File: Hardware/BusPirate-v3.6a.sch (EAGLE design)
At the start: 45 parts, among them J1 USB-MINIB-5PIN, U1 MIC5205 3V3, U2 MIC5205 3V3, U3 PIC24FJ64GA002, U4 MIC5205 5V0, U5 FT232RL-BASICSSOP, U6 4066

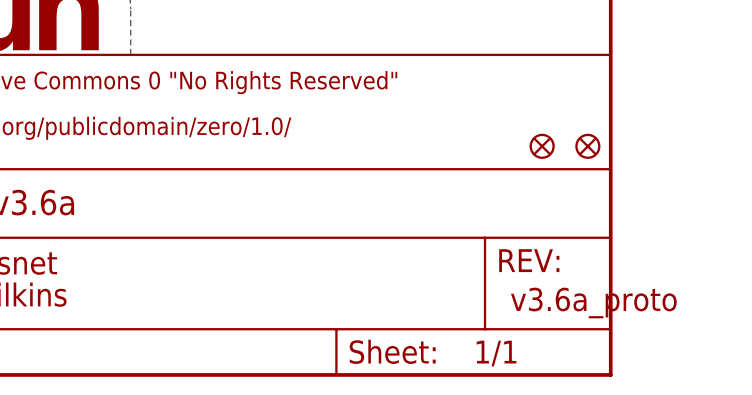
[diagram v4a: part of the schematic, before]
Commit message: Imported DP PCB part, and changed DRC to allow mask to cover large vias.
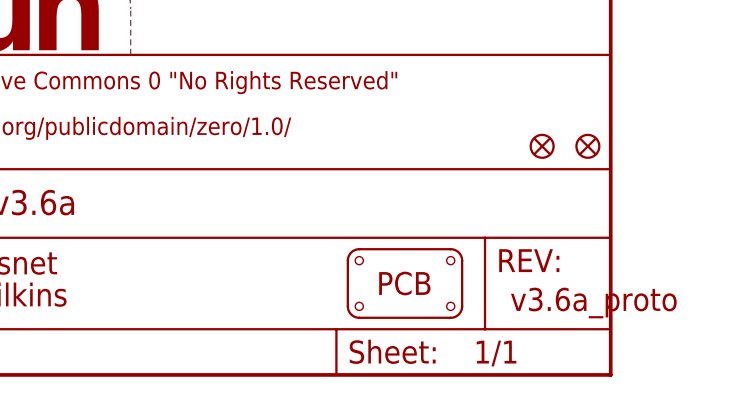
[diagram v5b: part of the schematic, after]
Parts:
- added PCB1: PCB_DP_RECTANGLE-37X60, SparkFun-Boards:PCB_DP_RECTANGLE-37X60
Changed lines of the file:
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@@
 <layer number="113" name="IDFDebug" color="4" fill="1" visible="yes" active="yes"/>
 <layer number="114" name="Badge_Outline" color="11" fill="1" visible="no" active="no"/>
+<layer number="115" name="ReferenceISLANDS" color="7" fill="1" visible="yes" active="yes"/>
 <layer number="116" name="Patch_BOT" color="9" fill="4" visible="yes" active="yes"/>
 <layer number="118" name="Rect_Pads" color="7" fill="1" visible="yes" active="yes"/>
@@
 <part name="C4" library="SparkFun-Capacitors" deviceset="10UF10V10%(0805)" device="" value="10uF"/>
 <part name="GND19" library="SparkFun-Aesthetics" deviceset="GND" device=""/>
+<part name="PCB1" library="SparkFun-Boards" deviceset="PCB_DP_RECTANGLE" device="-37X60"/>
 </parts>
 <sheets>
@@
 <instance part="C4" gate="G$1" x="30.48" y="114.3"/>
 <instance part="GND19" gate="1" x="109.22" y="15.24" rot="MR0"/>
+<instance part="PCB1" gate="G$1" x="226.06" y="10.16"/>
 </instances>
 <busses>

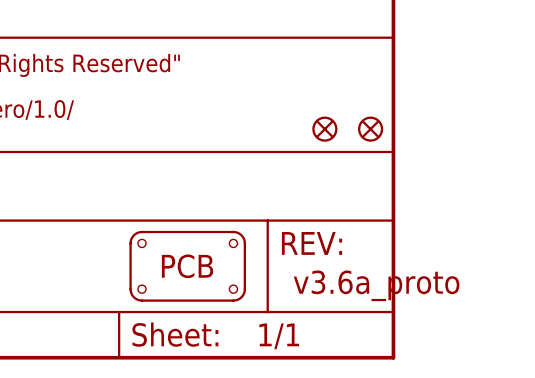
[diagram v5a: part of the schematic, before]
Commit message: Changed one PROD_ID and version number
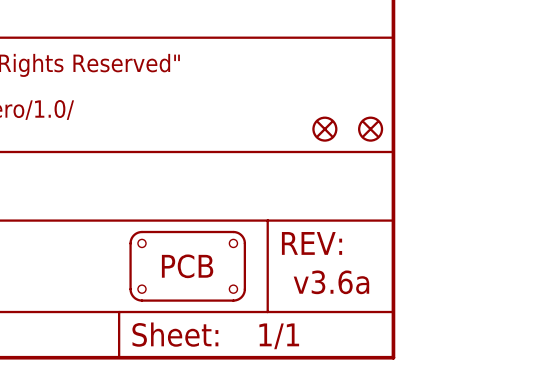
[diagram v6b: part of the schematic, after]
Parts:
- U6: PROD_ID IC-09427 -> IC-13191
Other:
- note added: "v3.6a"
- note removed: "v3.6a_proto"
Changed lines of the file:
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@@
 </part>
 <part name="U6" library="40xx" deviceset="4066" device="">
-<attribute name="PROD_ID" value="IC-09427"/>
+<attribute name="PROD_ID" value="IC-13191"/>
 </part>
 <part name="GND15" library="SparkFun-Aesthetics" deviceset="GND" device=""/>
@@
 <text x="148.59" y="7.62" size="2.54" layer="94" font="vector">Revised by: Brent Wilkins</text>
 <text x="171.196" y="11.176" size="2.54" layer="94" font="vector">Ian Lesnet</text>
-<text x="237.744" y="7.112" size="2.54" layer="94" font="vector">v3.6a_proto</text>
+<text x="237.744" y="7.112" size="2.54" layer="94" font="vector">v3.6a</text>
 <text x="60.96" y="180.34" size="2.1844" layer="97" font="vector" ratio="15" align="bottom-center">VOLTAGE REGULATION</text>
 <wire x1="121.92" y1="52.07" x2="73.66" y2="52.07" width="0.1524" layer="97" style="shortdash"/>

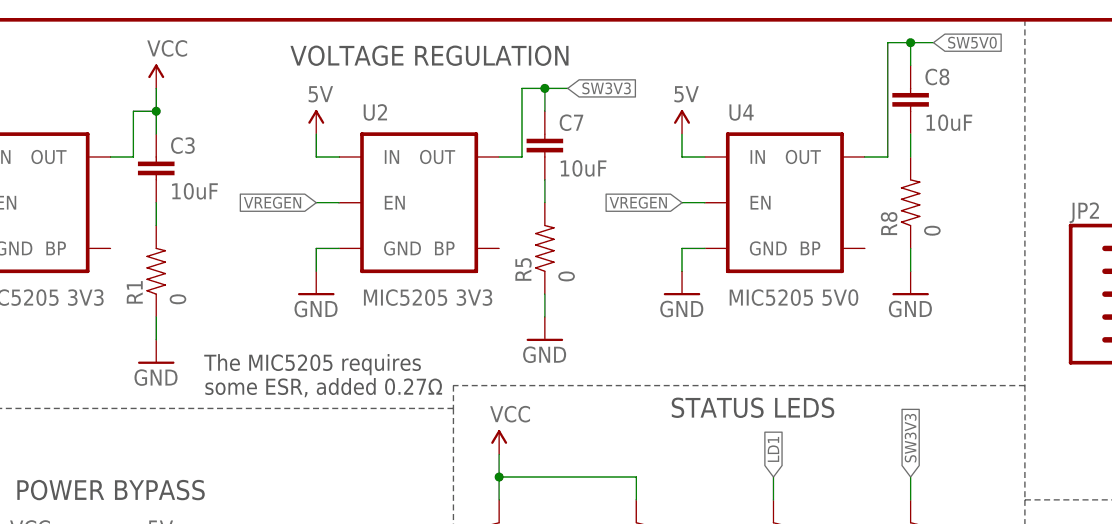
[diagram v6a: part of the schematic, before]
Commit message: Corrected resistor value
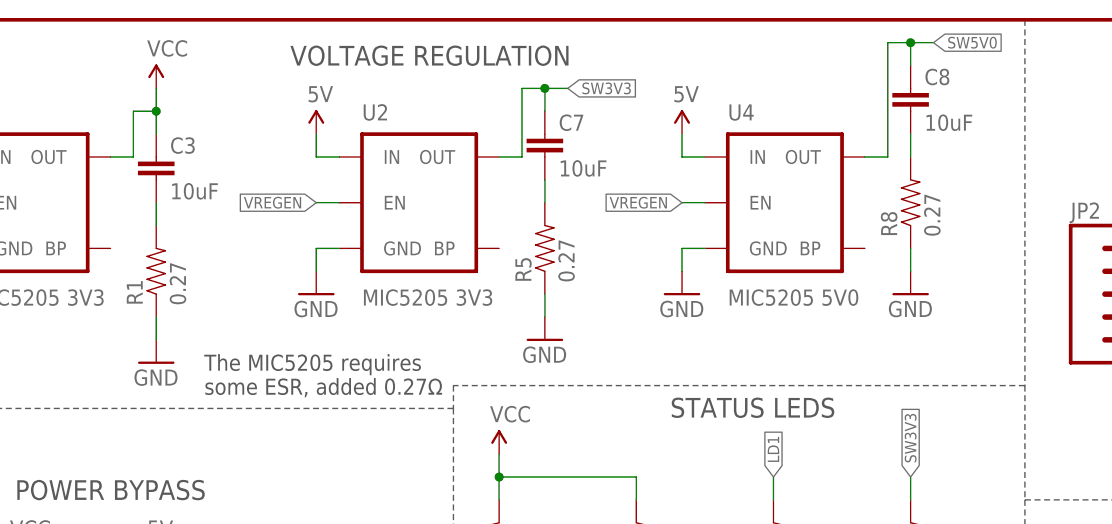
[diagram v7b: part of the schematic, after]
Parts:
- R1, R5, R8: value 0 -> 0.27
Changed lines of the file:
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@@
 <attribute name="PROD_ID" value="CONN-09508"/>
 </part>
-<part name="R1" library="SparkFun-Resistors" deviceset="0OHM-1/10W-5%(0603)" device="" value="0">
+<part name="R1" library="SparkFun-Resistors" deviceset="0OHM-1/10W-5%(0603)" device="" value="0.27">
 <attribute name="PROD_ID" value="RES-08787"/>
 </part>
-<part name="R5" library="SparkFun-Resistors" deviceset="0OHM-1/10W-5%(0603)" device="" value="0">
+<part name="R5" library="SparkFun-Resistors" deviceset="0OHM-1/10W-5%(0603)" device="" value="0.27">
 <attribute name="PROD_ID" value="RES-08787"/>
 </part>
-<part name="R8" library="SparkFun-Resistors" deviceset="0OHM-1/10W-5%(0603)" device="" value="0">
+<part name="R8" library="SparkFun-Resistors" deviceset="0OHM-1/10W-5%(0603)" device="" value="0.27">
 <attribute name="PROD_ID" value="RES-08787"/>
 </part>
